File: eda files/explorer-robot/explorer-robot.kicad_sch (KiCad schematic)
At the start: 0 parts

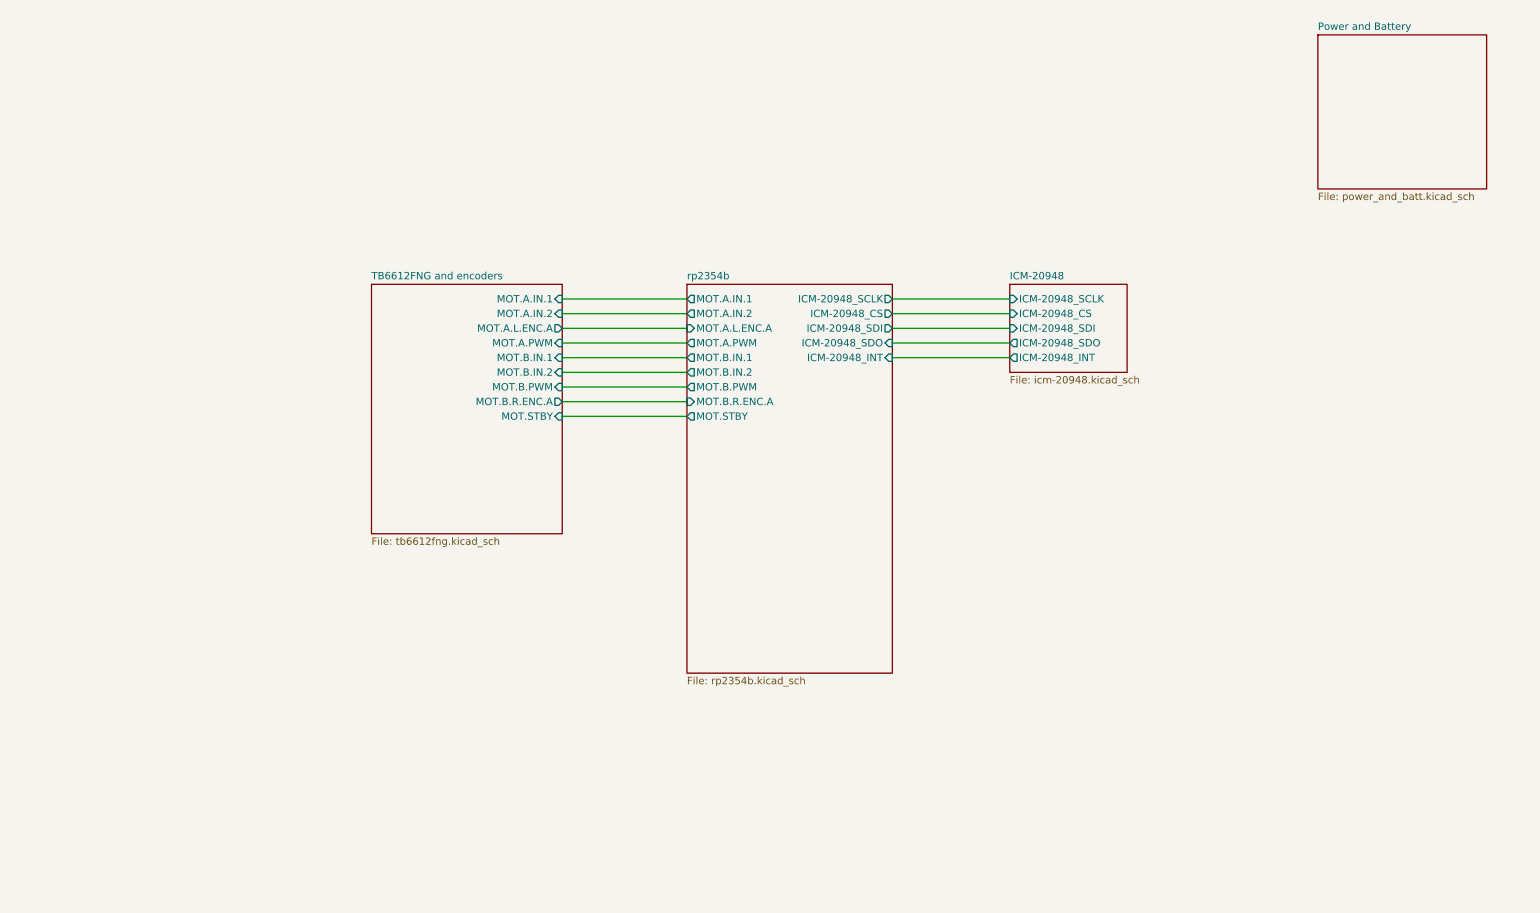
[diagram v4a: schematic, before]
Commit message: Add ADR-0021 for expansion UART and camera on PIO
Add an RGB LED connector sheet to the schematic.
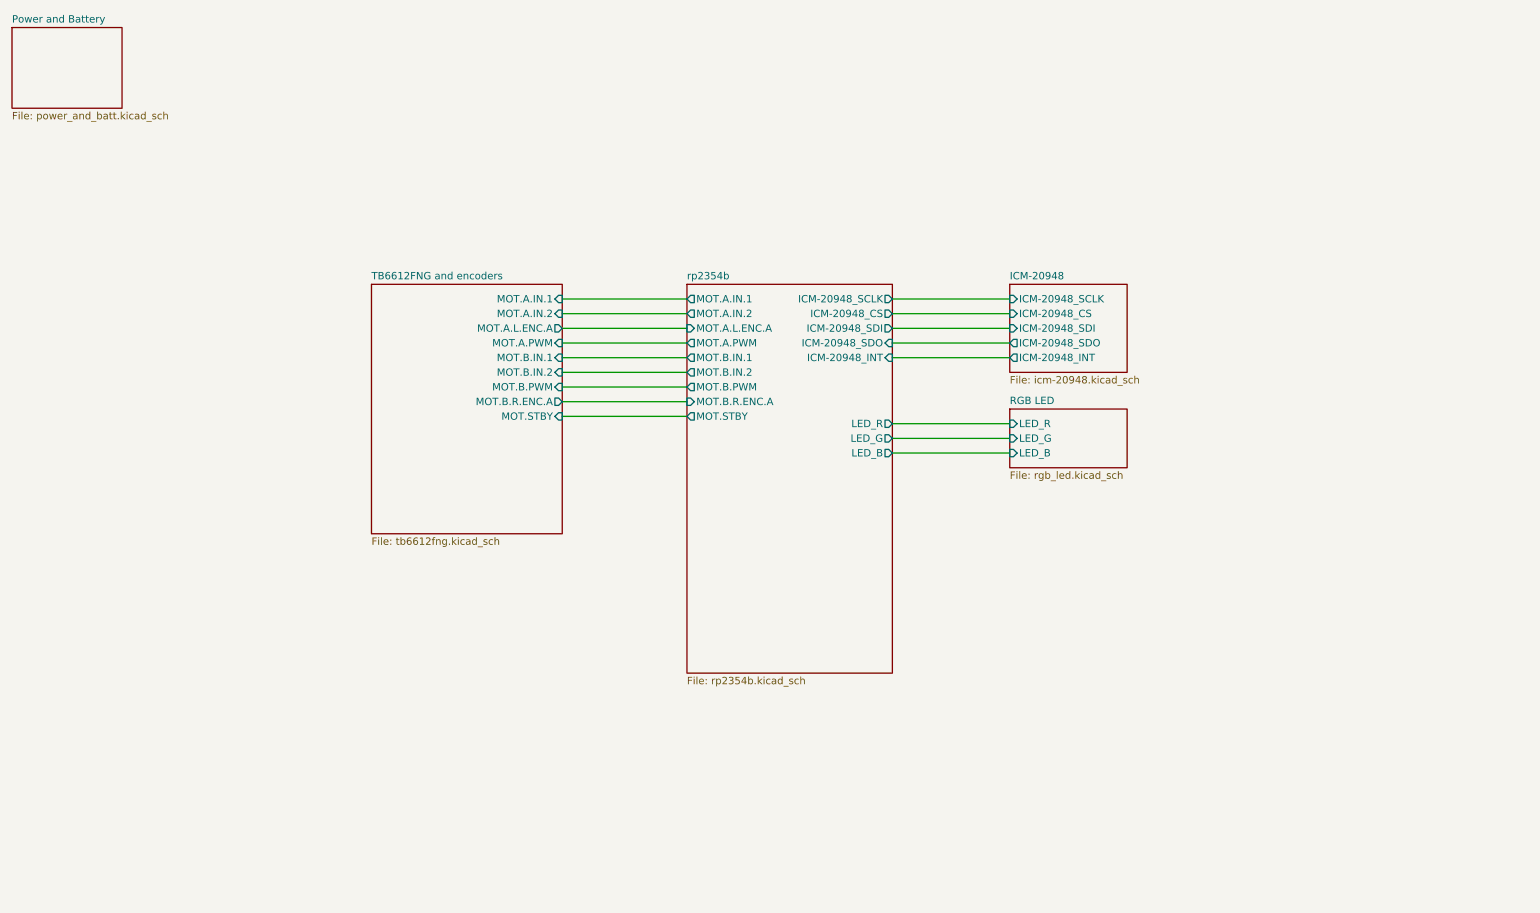
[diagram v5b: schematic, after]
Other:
- added sheet RGB LED (rgb_led.kicad_sch)
- sheet rp2354b ports: added LED_B, LED_G, LED_R; removed none
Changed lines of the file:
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@@
+	(wire
+		(pts
+			(xy 172.72 93.98) (xy 193.04 93.98)
+		)
+		(stroke
+			(width 0)
+			(type default)
+		)
+	)
 	(wire
 		(pts
@@
 	(wire
 		(pts
+			(xy 172.72 91.44) (xy 193.04 91.44)
+		)
+		(stroke
+			(width 0)
+			(type default)
+		)
+	)
+	(wire
+		(pts
 			(xy 115.57 87.63) (xy 137.16 87.63)
 		)
@@
 		(pts
 			(xy 115.57 69.85) (xy 137.16 69.85)
+		)
+		(stroke
+			(width 0)
+			(type default)
+		)
+	)
+	(wire
+		(pts
+			(xy 172.72 88.9) (xy 193.04 88.9)
 		)
 		(stroke
@@
 			)
 		)
+		(pin "LED_B" output
+			(at 172.72 93.98 0)
+			(effects
+				(font
+					(size 1.27 1.27)
+				)
+				(justify right)
+			)
+		)
+		(pin "LED_G" output
+			(at 172.72 91.44 0)
+			(effects
+				(font
+					(size 1.27 1.27)
+				)
+				(justify right)
+			)
+		)
+		(pin "LED_R" output
+			(at 172.72 88.9 0)
+			(effects
+				(font
+					(size 1.27 1.27)
+				)
+				(justify right)
+			)
+		)
 		(instances
 			(project "explorer-robot"
@@
 	)
 	(sheet
-		(at 246.38 21.59)
-		(size 29.21 26.67)
+		(at 193.04 86.36)
+		(size 20.32 10.16)
 		(exclude_from_sim no)
 		(in_bom yes)
@@
 			(color 0 0 0 0)
 		)
+		(property "Sheetname" "RGB LED"
+			(at 193.04 85.6484 0)
+			(show_name no)
+			(do_not_autoplace no)
+			(effects
+				(font
+					(size 1.27 1.27)
+				)
+				(justify left bottom)
+			)
+		)
+		(property "Sheetfile" "rgb_led.kicad_sch"
+			(at 193.04 97.1046 0)
+			(show_name no)
+			(do_not_autoplace no)
+			(effects
+				(font
+					(size 1.27 1.27)
+				)
+				(justify left top)
+			)
+		)
+		(pin "LED_B" input
+			(at 193.04 93.98 180)
+			(effects
+				(font
+					(size 1.27 1.27)
+				)
+				(justify left)
+			)
+		)
+		(pin "LED_G" input
+			(at 193.04 91.44 180)
+			(effects
+				(font
+					(size 1.27 1.27)
+				)
+				(justify left)
+			)
+		)
+		(pin "LED_R" input
+			(at 193.04 88.9 180)
+			(effects
+				(font
+					(size 1.27 1.27)
+				)
+				(justify left)
+			)
+		)
+		(instances
+			(project "explorer-robot"
+				(path "/57778957-dc0c-4e39-b470-8f64ada5e845"
+					(page "6")
+				)
+			)
+		)
+	)
+	(sheet
+		(at 20.32 20.32)
+		(size 19.05 13.97)
+		(exclude_from_sim no)
+		(in_bom yes)
+		(on_board yes)
+		(dnp no)
+		(fields_autoplaced yes)
+		(stroke
+			(width 0.1524)
+			(type solid)
+		)
+		(fill
+			(color 0 0 0 0)
+		)
 		(property "Sheetname" "Power and Battery"
-			(at 246.38 20.8784 0)
+			(at 20.32 19.6084 0)
 			(show_name no)
 			(do_not_autoplace no)
@@
 		)
 		(property "Sheetfile" "power_and_batt.kicad_sch"
-			(at 246.38 48.8446 0)
-			(show_name no)
-			(do_not_autoplace no)
+			(at 20.32 34.8746 0)
+			(show_name no)
+			(do_not_autoplace no)

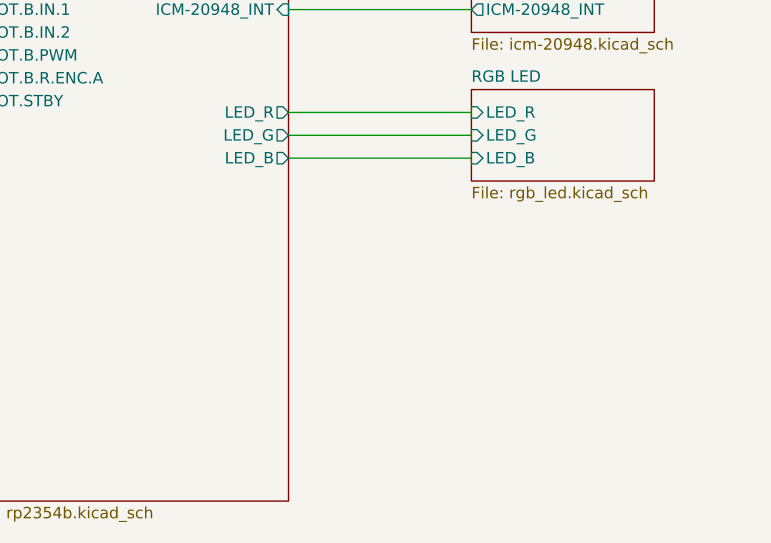
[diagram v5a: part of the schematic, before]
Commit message: Add LiDAR power and UART interface
Add a new lidar schematic sheet with a 4-pin connector, an
AO3400A low-side MOSFET for power switching, and gate pull
resistors. Wire LIDAR_PWR, LIDAR_TX, and LIDAR_RX hierarchical
labels into the MCU sheet and update designators.

Also shorten connector value labels to BAT, LED, and MBR.
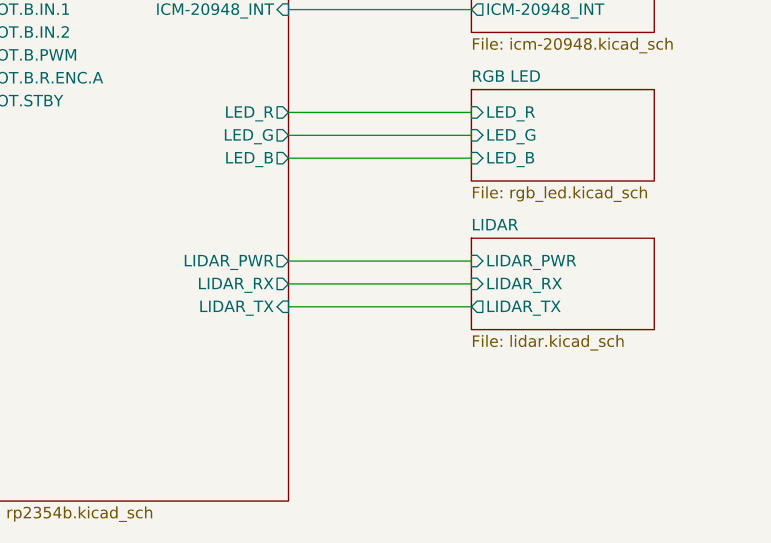
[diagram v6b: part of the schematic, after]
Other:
- added sheet LIDAR (lidar.kicad_sch)
- sheet rp2354b ports: added LIDAR_PWR, LIDAR_RX, LIDAR_TX; removed none
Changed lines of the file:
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@@
+	(wire
+		(pts
+			(xy 172.72 110.49) (xy 193.04 110.49)
+		)
+		(stroke
+			(width 0)
+			(type default)
+		)
+	)
+	(wire
+		(pts
+			(xy 172.72 105.41) (xy 193.04 105.41)
+		)
+		(stroke
+			(width 0)
+			(type default)
+		)
+	)
+	(wire
+		(pts
+			(xy 172.72 107.95) (xy 193.04 107.95)
+		)
+		(stroke
+			(width 0)
+			(type default)
+		)
+	)
 	(wire
 		(pts
@@
 			)
 		)
+		(pin "LIDAR_PWR" output
+			(at 172.72 105.41 0)
+			(effects
+				(font
+					(size 1.27 1.27)
+				)
+				(justify right)
+			)
+		)
+		(pin "LIDAR_RX" output
+			(at 172.72 107.95 0)
+			(effects
+				(font
+					(size 1.27 1.27)
+				)
+				(justify right)
+			)
+		)
+		(pin "LIDAR_TX" input
+			(at 172.72 110.49 0)
+			(effects
+				(font
+					(size 1.27 1.27)
+				)
+				(justify right)
+			)
+		)
 		(instances
 			(project "explorer-robot"
@@
 				)
 			)
+		)
+	)
+	(sheet
+		(at 193.04 102.87)
+		(size 20.32 10.16)
+		(exclude_from_sim no)
+		(in_bom yes)
+		(on_board yes)
+		(dnp no)
+		(fields_autoplaced yes)
+		(stroke
+			(width 0.1524)
+			(type solid)
+		)
+		(fill
+			(color 0 0 0 0)
+		)
+		(property "Sheetname" "LIDAR"
+			(at 193.04 102.1584 0)
+			(show_name no)
+			(do_not_autoplace no)
+			(effects
+				(font
+					(size 1.27 1.27)
+				)
+				(justify left bottom)
+			)
+		)
+		(property "Sheetfile" "lidar.kicad_sch"
+			(at 193.04 113.6146 0)
+			(show_name no)
+			(do_not_autoplace no)
+			(effects
+				(font
+					(size 1.27 1.27)
+				)
+				(justify left top)
+			)
+		)
+		(pin "LIDAR_PWR" input
+			(at 193.04 105.41 180)
+			(effects
+				(font
+					(size 1.27 1.27)
+				)
+				(justify left)
+			)
+		)
+		(pin "LIDAR_RX" input
+			(at 193.04 107.95 180)
+			(effects
+				(font
+					(size 1.27 1.27)
+				)
+				(justify left)
+			)
+		)
+		(pin "LIDAR_TX" output
+			(at 193.04 110.49 180)
+			(effects
+				(font
+					(size 1.27 1.27)
+				)
+				(justify left)
+			)
+		)
+		(instances
+			(project "explorer-robot"
+				(path "/57778957-dc0c-4e39-b470-8f64ada5e845"
+					(page "7")
+				)
+			)

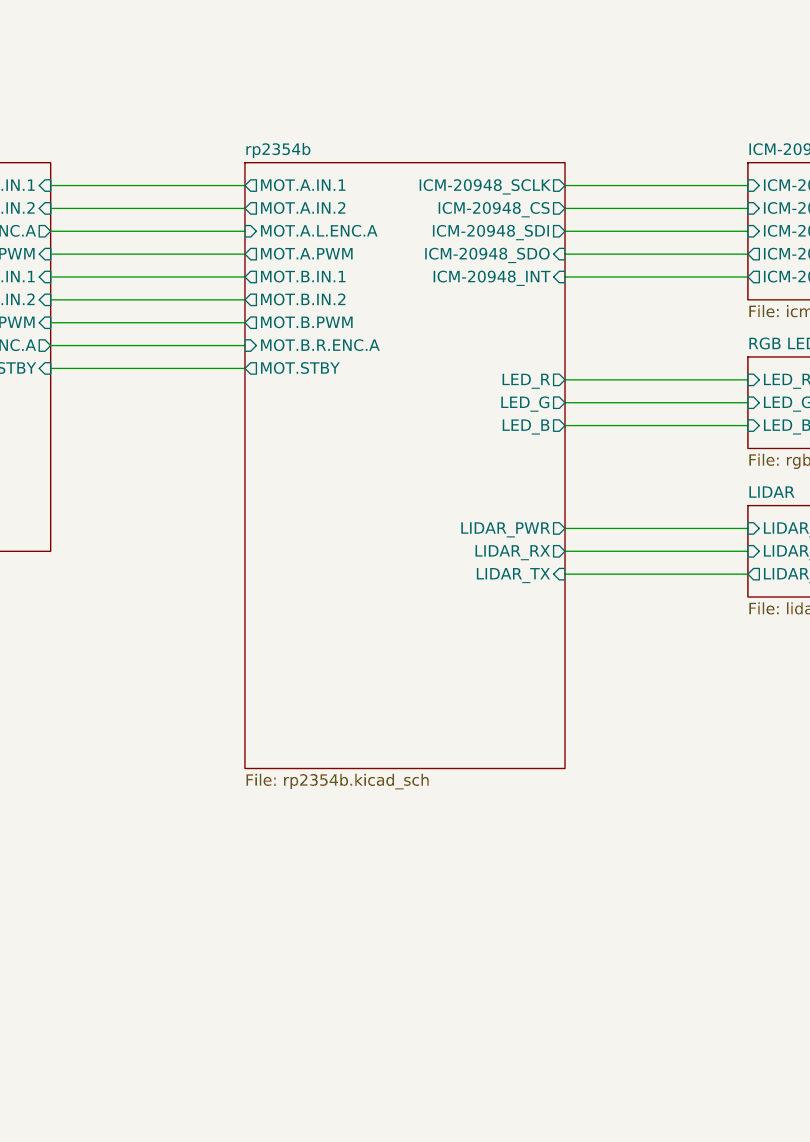
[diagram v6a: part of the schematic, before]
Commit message: Regroup RP2350B GPIOs by peripheral (ADR-0022)
Move motor/encoders to GPIO 4–12, LiDAR to 28–30, camera to 23–25
on a PIO0 UART, and reserve I2C1 on 26–27 for a second rangefinder.
Introduce assign_resources-based resource bundles so main splits the
embassy Peripherals in one call, and update docs, schematic and
firmware to the new pin map.
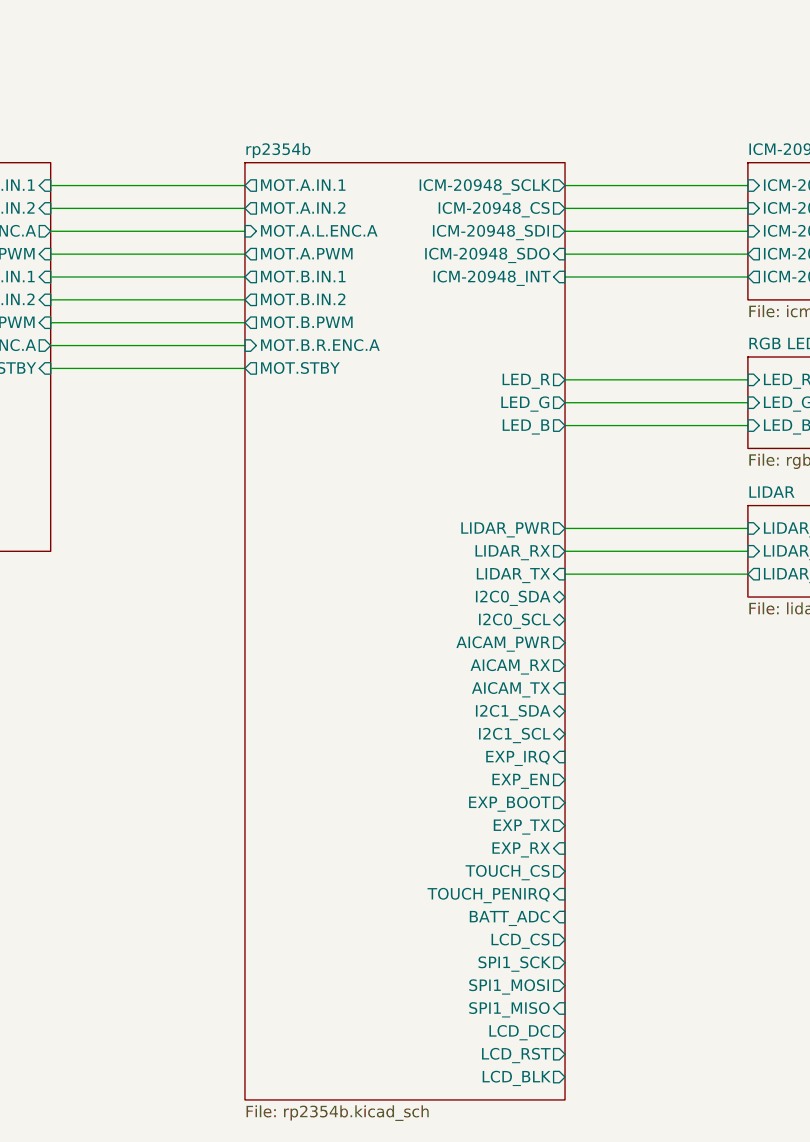
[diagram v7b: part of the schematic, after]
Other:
- sheet rp2354b ports: added AICAM_PWR, AICAM_RX, AICAM_TX, BATT_ADC, EXP_BOOT, EXP_EN, EXP_IRQ, EXP_RX, EXP_TX, I2C0_SCL, I2C0_SDA, I2C1_SCL, I2C1_SDA, LCD_BLK, LCD_CS, LCD_DC, LCD_RST, SPI1_MISO, SPI1_MOSI, SPI1_SCK, TOUCH_CS, TOUCH_PENIRQ; removed none
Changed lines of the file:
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@@
 	(sheet
 		(at 137.16 64.77)
-		(size 35.56 67.31)
+		(size 35.56 104.14)
 		(exclude_from_sim no)
 		(in_bom yes)
@@
 		)
 		(property "Sheetfile" "rp2354b.kicad_sch"
-			(at 137.16 132.6646 0)
+			(at 137.16 169.5 0)
 			(show_name no)
 			(do_not_autoplace no)
@@
 			(effects
 				(font
+					(size 1.27 1.27)
+				)
+				(justify right)
+			)
+		)
+		(pin "I2C0_SDA" bidirectional
+			(at 172.72 113.03 0)
+			(effects
+				(font
+					(size 1.27 1.27)
+				)
+				(justify right)
+			)
+		)
+		(pin "I2C0_SCL" bidirectional
+			(at 172.72 115.57 0)
+			(effects
+				(font
+					(size 1.27 1.27)
+				)
+				(justify right)
+			)
+		)
+		(pin "AICAM_PWR" output
+			(at 172.72 118.11 0)
+			(effects
+				(font
+					(size 1.27 1.27)
+				)
+				(justify right)
+			)
+		)
+		(pin "AICAM_RX" output
+			(at 172.72 120.65 0)
+			(effects
+				(font
+					(size 1.27 1.27)
+				)
+				(justify right)
+			)
+		)
+		(pin "AICAM_TX" input
+			(at 172.72 123.19 0)
+			(effects
+				(font
+					(size 1.27 1.27)
+				)
+				(justify right)
+			)
+		)
+		(pin "I2C1_SDA" bidirectional
+			(at 172.72 125.73 0)
+			(effects
+				(font
+					(size 1.27 1.27)
+				)
+				(justify right)
+			)
+		)
+		(pin "I2C1_SCL" bidirectional
+			(at 172.72 128.27 0)
+			(effects
+				(font
+					(size 1.27 1.27)
+				)
+				(justify right)
+			)
+		)
+		(pin "EXP_IRQ" input
+			(at 172.72 130.81 0)
+			(effects
+				(font
+					(size 1.27 1.27)
+				)
+				(justify right)
+			)
+		)
+		(pin "EXP_EN" output
+			(at 172.72 133.35 0)
+			(effects
+				(font
+					(size 1.27 1.27)
+				)
+				(justify right)
+			)
+		)
+		(pin "EXP_BOOT" output
+			(at 172.72 135.89 0)
+			(effects
+				(font
+					(size 1.27 1.27)
+				)
+				(justify right)
+			)
+		)
+		(pin "EXP_TX" output
+			(at 172.72 138.43 0)
+			(effects
+				(font
+					(size 1.27 1.27)
+				)
+				(justify right)
+			)
+		)
+		(pin "EXP_RX" input
+			(at 172.72 140.97 0)
+			(effects
+				(font
+					(size 1.27 1.27)
+				)
+				(justify right)
+			)
+		)
+		(pin "TOUCH_CS" output
+			(at 172.72 143.51 0)
+			(effects
+				(font
+					(size 1.27 1.27)
+				)
+				(justify right)
+			)
+		)
+		(pin "TOUCH_PENIRQ" input
+			(at 172.72 146.05 0)
+			(effects
+				(font
+					(size 1.27 1.27)
+				)
+				(justify right)
+			)
+		)
+		(pin "BATT_ADC" input
+			(at 172.72 148.59 0)
+			(effects
+				(font
+					(size 1.27 1.27)
+				)
+				(justify right)
+			)
+		)
+		(pin "LCD_CS" output
+			(at 172.72 151.13 0)
+			(effects
+				(font
+					(size 1.27 1.27)
+				)
+				(justify right)
+			)
+		)
+		(pin "SPI1_SCK" output
+			(at 172.72 153.67 0)
+			(effects
+				(font
+					(size 1.27 1.27)
+				)
+				(justify right)
+			)
+		)
+		(pin "SPI1_MOSI" output
+			(at 172.72 156.21 0)
+			(effects
+				(font
+					(size 1.27 1.27)
+				)
+				(justify right)
+			)
+		)
+		(pin "SPI1_MISO" input
+			(at 172.72 158.75 0)
+			(effects
+				(font
+					(size 1.27 1.27)
+				)
+				(justify right)
+			)
+		)
+		(pin "LCD_DC" output
+			(at 172.72 161.29 0)
+			(effects
+				(font
+					(size 1.27 1.27)
+				)
+				(justify right)
+			)
+		)
+		(pin "LCD_RST" output
+			(at 172.72 163.83 0)
+			(effects
+				(font
+					(size 1.27 1.27)
+				)
+				(justify right)
+			)
+		)
+		(pin "LCD_BLK" output
+			(at 172.72 166.37 0)
+			(effects
+				(font

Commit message: Add sheet titles and tidy RP2354B schematic layout
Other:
- title: (none) -> System Overview and main connections
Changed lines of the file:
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@@
 	(paper "A4")
 	(title_block
+		(title "System Overview and main connections")
 		(date "2026-09-27")
 		(rev "v.0.1")
@@
 	(sheet
 		(at 82.55 64.77)
-		(size 33.02 43.18)
+		(size 33.02 25.4)
 		(exclude_from_sim no)
 		(in_bom yes)
@@
 		)
 		(property "Sheetfile" "tb6612fng.kicad_sch"
-			(at 82.55 108.5346 0)
+			(at 82.55 90.7546 0)
 			(show_name no)
 			(do_not_autoplace no)
